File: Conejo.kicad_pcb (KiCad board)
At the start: 4 copper layers, 130.3 x 112.5 mm, 105 parts, among them J1 BATT, J2 HRO_TYPE-C-31-M-12, J3 JTAG_TC2030, J4 RGB, Q1 2N7002, Q2 2N7002, Q3 AO3407, SW1 POWER, SW10 MX Hotswap, SW11 MX Hotswap, SW12 MX Hotswap, SW13 MX Hotswap, SW14 MX Hotswap, SW15 MX Hotswap, SW16 MX Hotswap, SW17 MX Hotswap, SW18 MX Hotswap, SW19 MX Hotswap, SW2 MX Hotswap, SW20 MX Hotswap, SW21 MX Hotswap, SW22 MX Hotswap, SW23 MX Hotswap, SW24 MX Hotswap, SW25 MX Hotswap, SW26 MX Hotswap, SW27 MX Hotswap, SW28 MX Hotswap, SW29 RESET, SW3 MX Hotswap, SW4 MX Hotswap, SW5 MX Hotswap, SW6 MX Hotswap, SW7 MX Hotswap, SW8 MX Hotswap, SW9 MX Hotswap, U1 BQ24075RGT, U2 MAX17048, U3 SRV05-4, U4 MS88SF3

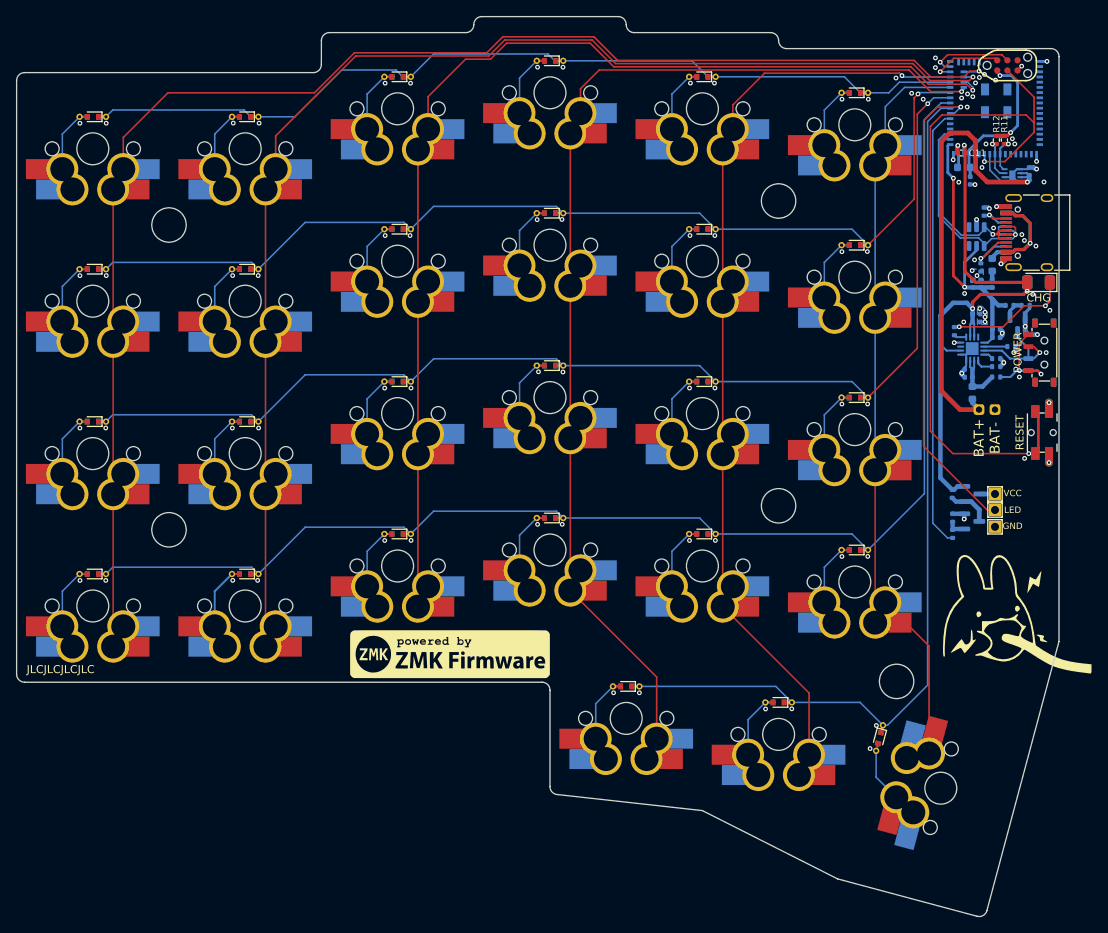
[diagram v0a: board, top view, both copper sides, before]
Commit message: feat(pcb): Version 0.3
- Move components entirely to back copper :tada:
- Update silkscreen legibility to enhance ease of component placement
- Fix I2C pullup resistors
  - Replace incorrect value of 1K5 with 5K1
  - Update footprint to 0603_1608 to fit VDD traces underneath, compared to original 0402_1005 footprint
- Increase text width on RESET button, POWER Switch, and CHG LED
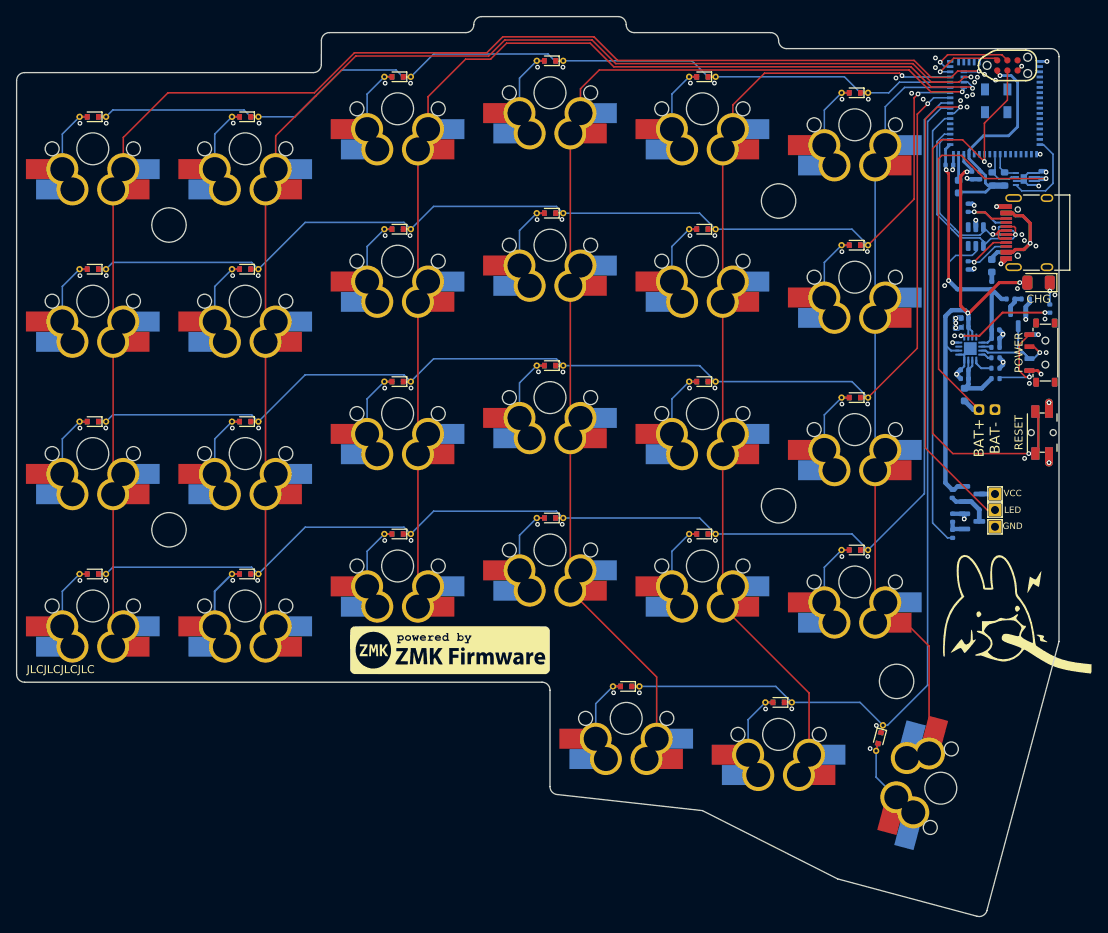
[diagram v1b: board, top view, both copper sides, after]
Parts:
- removed C11: 100nF, Capacitor_SMD:C_0402_1005Metric
- C1, C10, C4, C6, C8: value 4.7uF -> 4u7F
- C9: value 1uF -> 4u7F
- D1: moved to B.Cu
- FB1: value 120@100MHz -> 120R@100MHz
- L1: value NC -> 10uH
- R11, R12: value 1K5 -> 5K1; footprint Resistor_SMD:R_0402_1005Metric -> Resistor_SMD:R_0603_1608Metric; moved to B.Cu
- R3: renamed from R5; value 100K -> 10K
- R6: value 10K -> 100K
- moved C9 13.5 mm to (109.9, 5.33)
- moved C8 13.5 mm to (110.9, 5.33)
- moved R7 12.3 mm to (119.6, 22.0)
- moved R12 4.90 mm to (112.4, 5.78), turned to -90 degrees
- moved R11 4.88 mm to (114.0, 5.78), turned to -90 degrees
- moved C10 3.25 mm to (107.1, 4.03), turned to 0 degrees
- moved L1 2.49 mm to (108.2, 6.72), turned to -90 degrees
- moved R8 2.06 mm to (109.4, 9.38)
- moved R1 1.99 mm to (112.8, 26.8)
- moved C4 1.62 mm to (109.0, 24.3), turned to 180 degrees
- moved R9 1.59 mm to (109.4, 16.6)
- moved C3 1.58 mm to (109.0, 23.2), turned to 180 degrees
- moved C5 1.54 mm to (118.5, 5.28)
- moved R6 1.50 mm to (112.8, 30.7)
- moved U2 1.50 mm to (116.4, 5.78)
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- renumbered C5 to C3, C3 to C5, R3 to R1, R4 to R2, R1 to R4, R2 to R5
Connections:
- C10 pad 1: VDD -> +5V
- C8 pad 1: GND -> VDD
- C8 pad 2: +5V -> GND
- C9 pad 1: GND -> VDDH
- C9 pad 2: +5V -> GND
- R3 pad 1: Net-(R5-Pad1) -> GND
- R3 pad 2: VBAT -> /Power Management/TS
- R6 pad 1: GND -> Net-(R6-Pad1)
- R6 pad 2: /Power Management/TS -> VBAT
- SW1 pad 3: Net-(R5-Pad1) -> Net-(R6-Pad1)
- U4 pad 17: unconnected-(U4-Pad17) -> ALERT
- U4 pad 27: ALERT -> unconnected-(U4-Pad27)
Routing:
- net Net-(D1-Pad1): track 18.8 -> 3.83 mm, vias 2 -> 1
- net RESET: track 93.9 -> 80.9 mm
- net /Power Management/CHG: track 1.57 -> 12.8 mm, vias 0 -> 2
- net Net-(R6-Pad1): track 0.00 -> 11.2 mm, vias 0 -> 1
- net Net-(R5-Pad1): track 10.2 -> 0.00 mm, vias 1 -> 0
- net VDDH: track 73.3 -> 65.1 mm
- net VDD: track 21.4 -> 28.4 mm, vias 2 -> 1
- net ALERT: track 4.39 -> 11.1 mm
- net /USB-C/CC2: track 5.48 -> 9.68 mm
- net +BATT: track 57.8 -> 53.7 mm
- net GND: track 38.7 -> 41.2 mm, vias 113 -> 105
- net /USB-C/CC1: track 8.40 -> 10.7 mm
- net /Power Management/TMR: track 2.95 -> 1.24 mm
- net +5V: track 38.2 -> 39.8 mm
- net DCCH: track 1.71 -> 3.26 mm
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
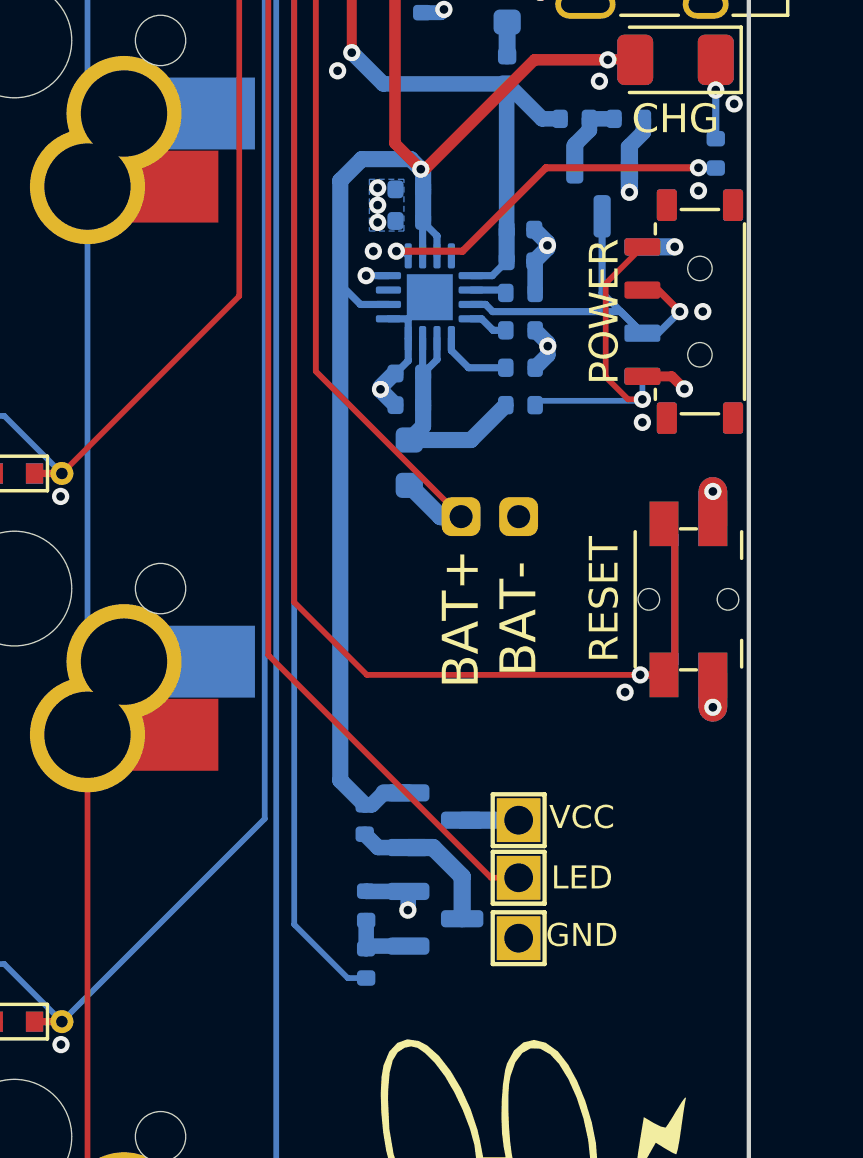
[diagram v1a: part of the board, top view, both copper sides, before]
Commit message: fix(pcb): Update RGB header component placement
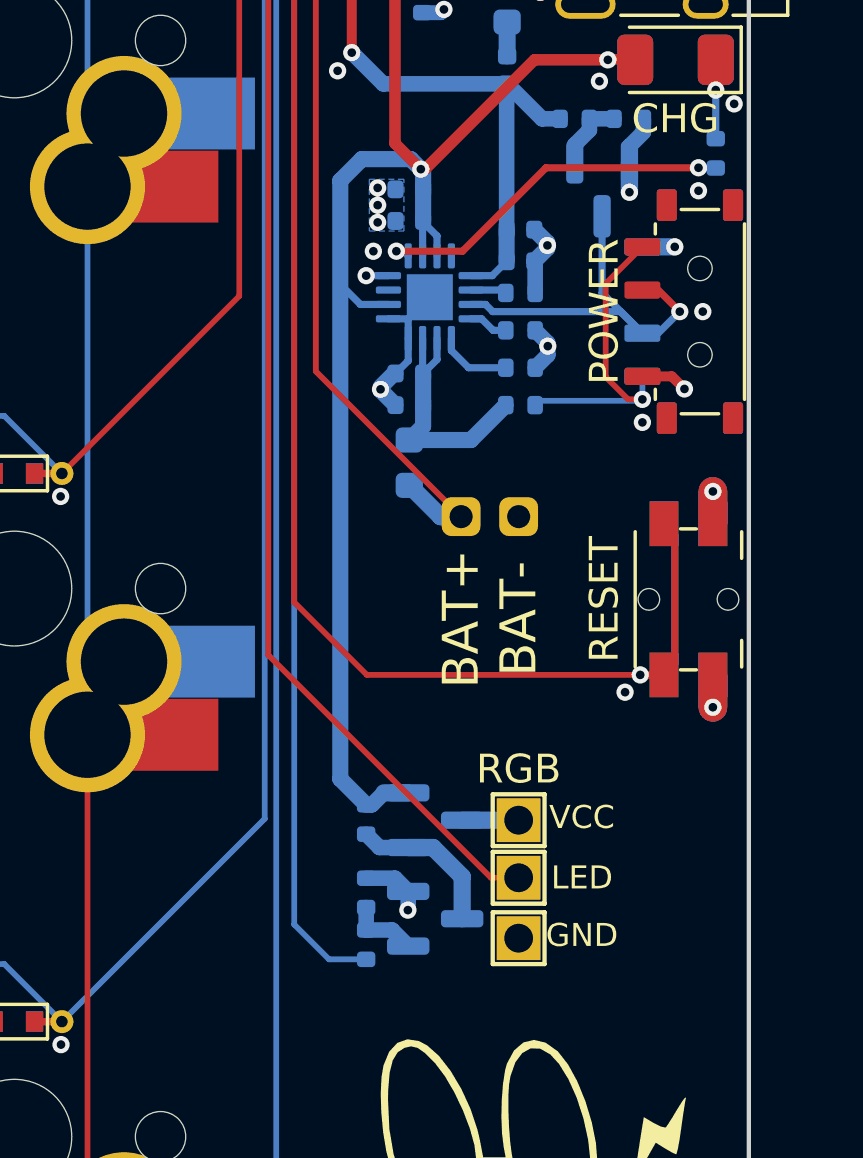
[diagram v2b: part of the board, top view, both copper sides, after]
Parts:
- moved R10 0.65 mm to (107.5, 49.5)
- moved R13 0.45 mm to (107.5, 47.7)
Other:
- board text added: "RGB"
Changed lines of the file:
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@@
   )
   (footprint "Resistor_SMD:R_0402_1005Metric" (layer "B.Cu")
-    (at 107.475 48.125001 -90)
+    (at 107.475 47.675 -90)
     (descr "Resistor SMD 0402 (1005 Metric), square (rectangular) end terminal, IPC_7351 nominal, (Body size source: IPC-SM-782 page 72, https://www.pcb-3d.com/wordpress/wp-content/uploads/ipc-sm-782a_amendment_1_and_2.pdf), generated with kicad-footprint-generator")
     (tags "resistor")
@@
     (property "Sheetname" "nRF52840 Module")
     (attr smd)
-    (fp_text reference "R13" (at 0 1.575) (layer "B.SilkS")
+    (fp_text reference "R13" (at -0.000001 1.6) (layer "B.SilkS")
       (effects (font (size 0.8 0.8) (thickness 0.15)) (justify mirror))
     )
@@
   )
   (footprint "Resistor_SMD:R_0402_1005Metric" (layer "B.Cu")
-    (at 107.475 50.125 90)
+    (at 107.475 49.475 90)
     (descr "Resistor SMD 0402 (1005 Metric), square (rectangular) end terminal, IPC_7351 nominal, (Body size source: IPC-SM-782 page 72, https://www.pcb-3d.com/wordpress/wp-content/uploads/ipc-sm-782a_amendment_1_and_2.pdf), generated with kicad-footprint-generator")
     (tags "resistor")
@@
     (property "Sheetname" "nRF52840 Module")
     (attr smd)
-    (fp_text reference "R10" (at 0 -1.5) (layer "B.SilkS")
+    (fp_text reference "R10" (at 0 -1.6) (layer "B.SilkS")
       (effects (font (size 0.8 0.8) (thickness 0.15)) (justify mirror))
     )
@@
   )
   (footprint "Resistor_SMD:R_0402_1005Metric" (layer "B.Cu")
-    (at 107.425 45.125 90)
+    (at 107.475 45.125 90)
     (descr "Resistor SMD 0402 (1005 Metric), square (rectangular) end terminal, IPC_7351 nominal, (Body size source: IPC-SM-782 page 72, https://www.pcb-3d.com/wordpress/wp-content/uploads/ipc-sm-782a_amendment_1_and_2.pdf), generated with kicad-footprint-generator")
     (tags "resistor")
@@
     (property "Sheetname" "nRF52840 Module")
     (attr smd)
-    (fp_text reference "R14" (at 0 -1.55) (layer "B.SilkS")
+    (fp_text reference "R14" (at 0 -1.6) (layer "B.SilkS")
       (effects (font (size 0.8 0.8) (thickness 0.15)) (justify mirror))
     )
@@
   (gr_line (start 120.775 63.575) (end 111.761384 97.224991) (layer "Edge.Cuts") (width 0.15))
   (gr_arc (start -9.525 -6.525) (mid -9.232107 -7.232107) (end -8.525 -7.525) (layer "Edge.Cuts") (width 0.15))
+  (gr_text "RGB" (at 112.825 43.375) (layer "B.SilkS")
+    (effects (font (size 1 1) (thickness 0.2)) (justify mirror))
+  )
   (gr_text "RESET" (at 115.75 37.325 90) (layer "B.SilkS")
     (effects (font (size 1 1) (thickness 0.2)) (justify mirror))
@@
     (effects (font (size 1 1) (thickness 0.2)) (justify left))
   )
+  (gr_text "RGB" (at 112.775 43.375) (layer "F.SilkS")
+    (effects (font (size 1 1) (thickness 0.2)))
+  )
   (gr_text "Pinky2	-> 	Pinky:	0mm\nPinky 	-> 	Ring:	5mm\nRing 	-> 	Middle:	2mm\nMiddle 	-> 	Index:	2mm\nIndex 	-> 	Index2:	2mm\n" (at -13.675 100.025) (layer "Cmts.User")
     (effects (font (size 1.5 1.5) (thickness 0.3)) (justify left))
@@
   (segment (start 119.024417 4.795) (end 118.525 4.795) (width 0.56) (layer "B.Cu") (net 2))
   (segment (start 117.3625 6.525) (end 116.907586 6.525) (width 0.25) (layer "B.Cu") (net 2))
-  (segment (start 108.9375 47.625) (end 107.485 47.624999) (width 0.54) (layer "B.Cu") (net 2))
   (segment (start 117.3625 5.025) (end 116.907586 5.025) (width 0.25) (layer "B.Cu") (net 2))
   (segment (start 109.275 5.676517) (end 109.403483 5.805) (width 0.35) (layer "B.Cu") (net 2))
@@
   (segment (start 117.3625 5.025) (end 118.295 5.025) (width 0.25) (layer "B.Cu") (net 2))
   (segment (start 113.7875 28.675) (end 113.7875 28.985) (width 0.54) (layer "B.Cu") (net 2))
-  (segment (start 107.485 47.624999) (end 107.475 47.615) (width 0.54) (layer "B.Cu") (net 2))
   (segment (start 113.7875 28.985) (end 113.3475 29.425) (width 0.54) (layer "B.Cu") (net 2))
   (segment (start 113.775 25.0825) (end 113.3175 24.625) (width 0.56) (layer "B.Cu") (net 2))
@@
   (segment (start 107.575 2.675) (end 107.575 4.005) (width 0.35) (layer "B.Cu") (net 2))
   (segment (start 113.775 25.175) (end 113.775 25.2675) (width 0.56) (layer "B.Cu") (net 2))
+  (segment (start 108.9375 47.625) (end 108.4775 47.165) (width 0.54) (layer "B.Cu") (net 2))
   (segment (start 108.495 29.625) (end 108.9375 29.1825) (width 0.25) (layer "B.Cu") (net 2))
   (segment (start 107.575 4.005) (end 107.555 4.025) (width 0.35) (layer "B.Cu") (net 2))
@@
   (segment (start 117.11 20.775) (end 117.11 21.24) (width 0.54) (layer "B.Cu") (net 2))
   (segment (start 110.175 9.075497) (end 109.964503 8.865) (width 0.54) (layer "B.Cu") (net 2))
+  (segment (start 108.4775 47.165) (end 107.475 47.165) (width 0.54) (layer "B.Cu") (net 2))
   (segment (start 108.9375 29.1825) (end 108.9375 28.4125) (width 0.25) (layer "B.Cu") (net 2))
   (segment (start 109.875 5.805) (end 110.875 5.805) (width 0.56) (layer "B.Cu") (net 2))
@@
   (segment (start 107.275 27.225) (end 108.250001 27.225) (width 0.25) (layer "B.Cu") (net 50))
   (segment (start 106.575 26.525) (end 107.275 27.225) (width 0.25) (layer "B.Cu") (net 50))
-  (segment (start 107.675 44.615) (end 107.425 44.615) (width 0.54) (layer "B.Cu") (net 50))
   (segment (start 109.4375 25.5375) (end 109.4375 24.345) (width 0.25) (layer "B.Cu") (net 50))
   (segment (start 108.875 3.625) (end 109.875 4.625) (width 0.35) (layer "B.Cu") (net 50))
-  (segment (start 106.575 43.765) (end 107.425 44.615) (width 0.56) (layer "B.Cu") (net 50))
   (segment (start 108.937499 44.2) (end 108.09 44.2) (width 0.6) (layer "B.Cu") (net 50))
-  (segment (start 109.025 22.175) (end 107.325 22.175) (width 0.56) (layer "B.Cu") (net 50))
+  (segment (start 107.675 44.615) (end 107.475 44.615) (width 0.54) (layer "B.Cu") (net 50))
   (segment (start 109.4375 24.345) (end 109.9375 24.845) (width 0.25) (layer "B.Cu") (net 50))
+  (segment (start 109.025 22.175) (end 107.325 22.175) (width 0.56) (layer "B.Cu") (net 50))
   (segment (start 109.375 22.525) (end 109.455 22.605) (width 0.56) (layer "B.Cu") (net 50))
+  (segment (start 107.325 22.175) (end 106.575 22.925) (width 0.56) (layer "B.Cu") (net 50))
   (segment (start 115.895 18.705) (end 116.825 18.705) (width 0.35) (layer "B.Cu") (net 50))
   (segment (start 109.875 4.625) (end 109.875 4.845) (width 0.35) (layer "B.Cu") (net 50))
   (segment (start 109.455 22.605) (end 109.455 23.225) (width 0.56) (layer "B.Cu") (net 50))
   (segment (start 109.307014 4.845) (end 109.875 4.845) (width 0.4) (layer "B.Cu") (net 50))
-  (segment (start 109.375 22.525) (end 109.025 22.175) (width 0.56) (layer "B.Cu") (net 50))
+  (segment (start 106.575 43.715) (end 107.475 44.615) (width 0.56) (layer "B.Cu") (net 50))
   (segment (start 115.875 18.725) (end 115.895 18.705) (width 0.35) (layer "B.Cu") (net 50))
   (segment (start 109.455 24.325) (end 109.455 23.225) (width 0.56) (layer "B.Cu") (net 50))
-  (segment (start 106.575 22.925) (end 106.575 43.765) (width 0.56) (layer "B.Cu") (net 50))
   (segment (start 109.275 4.877014) (end 109.307014 4.845) (width 0.4) (layer "B.Cu") (net 50))
+  (segment (start 106.575 22.925) (end 106.575 43.715) (width 0.56) (layer "B.Cu") (net 50))
   (segment (start 108.09 44.2) (end 107.675 44.615) (width 0.54) (layer "B.Cu") (net 50))
-  (segment (start 107.325 22.175) (end 106.575 22.925) (width 0.56) (layer "B.Cu") (net 50))
   (segment (start 108.875 2.675) (end 108.875 3.625) (width 0.35) (layer "B.Cu") (net 50))
+  (segment (start 109.375 22.525) (end 109.025 22.175) (width 0.56) (layer "B.Cu") (net 50))
   (segment (start 109.9375 28.4125) (end 109.9375 29.1425) (width 0.25) (layer "B.Cu") (net 51))
   (segment (start 109.455 30.725) (end 109.455 31.4575) (width 0.56) (layer "B.Cu") (net 51))
@@
   (segment (start 119.625 18.705) (end 119.625 21.465) (width 0.25) (layer "B.Cu") (net 105))
   (segment (start 110.8125 45.15) (end 112.8 45.15) (width 0.6) (layer "B.Cu") (net 106))
-  (segment (start 107.565 49.525) (end 107.475 49.615) (width 0.54) (layer "B.Cu") (net 107))
-  (segment (start 108.9375 49.525) (end 107.565 49.525) (width 0.54) (layer "B.Cu") (net 107))
-  (segment (start 107.475 49.615) (end 107.474999 48.635) (width 0.54) (layer "B.Cu") (net 107))
+  (segment (start 107.475 48.965) (end 108.3775 48.965) (width 0.54) (layer "B.Cu") (net 107))
+  (segment (start 108.3775 48.965) (end 108.9375 49.525) (width 0.54) (layer "B.Cu") (net 107))
+  (segment (start 107.475 48.185) (end 107.475 48.965) (width 0.54) (layer "B.Cu") (net 107))
+  (segment (start 108.9375 46.1) (end 107.94 46.1) (width 0.54) (layer "B.Cu") (net 108))
+  (segment (start 107.94 46.1) (end 107.475 45.635) (width 0.54) (layer "B.Cu") (net 108))
   (segment (start 109.8 46.1) (end 108.9375 46.1) (width 0.6) (layer "B.Cu") (net 108))
-  (segment (start 107.89 46.1) (end 107.425 45.635) (width 0.54) (layer "B.Cu") (net 108))
-  (segment (start 108.9375 46.1) (end 107.89 46.1) (width 0.54) (layer "B.Cu") (net 108))
   (segment (start 110.8125 48.575) (end 110.8125 47.1125) (width 0.6) (layer "B.Cu") (net 108))
   (segment (start 110.8125 47.1125) (end 109.8 46.1) (width 0.6) (layer "B.Cu") (net 108))
-  (segment (start 106.835 50.635) (end 104.975 48.775) (width 0.2) (layer "B.Cu") (net 109))
-  (segment (start 107.475001 50.635) (end 106.835 50.635) (width 0.2) (layer "B.Cu") (net 109))
   (segment (start 104.975 48.775) (end 104.975 -0.249022) (width 0.2) (layer "B.Cu") (net 109))
+  (segment (start 106.185 49.985) (end 104.975 48.775) (width 0.2) (layer "B.Cu") (net 109))
+  (segment (start 107.475 49.985) (end 106.185 49.985) (width 0.2) (layer "B.Cu") (net 109))
   (segment (start 104.975 -0.249022) (end 106.500978 -1.775) (width 0.2) (layer "B.Cu") (net 109))
   (segment (start 106.500978 -1.775) (end 107.175 -1.775) (width 0.2) (layer "B.Cu") (net 109))

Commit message: feat(pcb): Version 0.3.1
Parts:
- U4: footprint Conejo:MS88SF3_PeteJohanson -> Conejo:MS88SF3_V2
- moved J3 57.3 mm to (57.1, -12.0), turned to 180 degrees
- moved D5 8.92 mm to (-8.32, 39.3), turned to -90 degrees
- moved D14 8.92 mm to (29.8, 53.4), turned to -90 degrees
- moved D23 8.92 mm to (67.9, 53.4), turned to -90 degrees
- moved D28 8.92 mm to (86.9, 55.4), turned to -90 degrees
- moved D10 8.92 mm to (10.7, 58.4), turned to -90 degrees
- moved D11 8.92 mm to (29.8, -3.80), turned to -90 degrees
- moved D20 8.92 mm to (67.9, -3.80), turned to -90 degrees
- moved D21 8.92 mm to (67.9, 15.2), turned to -90 degrees
- moved D25 8.92 mm to (86.9, -1.80), turned to -90 degrees
- moved D26 8.92 mm to (86.9, 17.2), turned to -90 degrees
- moved D13 8.92 mm to (29.8, 34.3), turned to -90 degrees
- moved D22 8.92 mm to (67.9, 34.3), turned to -90 degrees
- moved D27 8.92 mm to (86.9, 36.3), turned to -90 degrees
- moved D3 8.92 mm to (-8.32, 1.20), turned to -90 degrees
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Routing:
- net RESET: track 80.9 -> 134.7 mm
- net VDD: track 28.4 -> 79.6 mm
- net SWCLK: track 10.5 -> 51.8 mm
- net SWDIO: track 9.19 -> 50.3 mm
- net ROW1: track 109.8 -> 122.5 mm
- net ROW3: track 144.9 -> 154.9 mm
- net ROW2: track 127.5 -> 137.6 mm
- net ROW5: track 114.1 -> 123.8 mm, vias 0 -> 1
- net ROW4: track 162.7 -> 172.4 mm, vias 0 -> 1
- net LED_MOSI: track 59.7 -> 67.7 mm, vias 1 -> 0
- net COL1: track 177.7 -> 170.2 mm
- net Net-(D10-Pad2): track 10.3 -> 5.21 mm
- net COL4: track 133.6 -> 130.1 mm
- net Net-(D14-Pad2): track 7.43 -> 5.20 mm
- net Net-(D5-Pad2): track 7.43 -> 5.21 mm
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- added copper zone on B.Cu, net +BATT
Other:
- board text removed: "JLCJLCJLCJLC"
